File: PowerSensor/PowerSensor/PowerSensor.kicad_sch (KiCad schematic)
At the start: 14 parts, among them J1 Current Sens, J3 BAT+, J4 BAT-, J5 Screw_Terminal_01x04, U1 ACS712ELCTR-20A-T_NRND

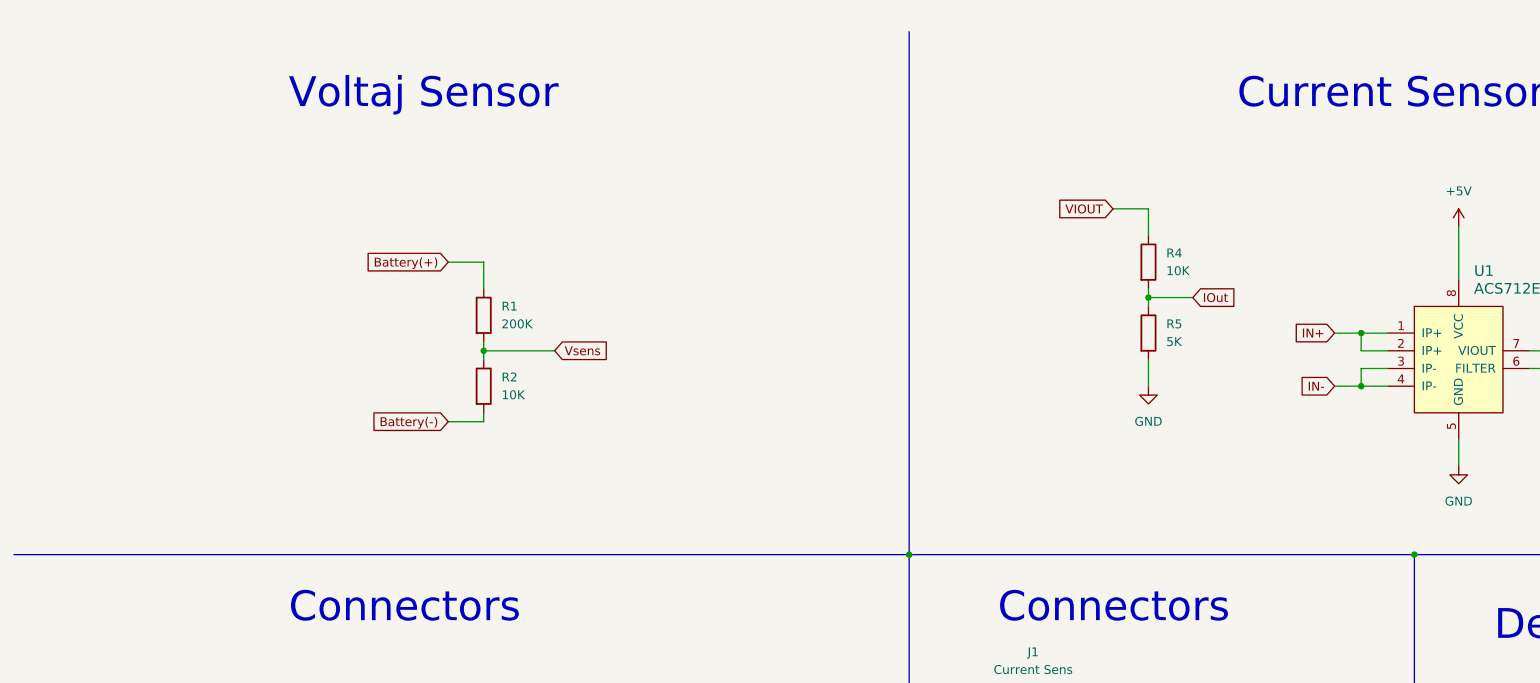
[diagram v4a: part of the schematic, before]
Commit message: Add discription for voltage divider
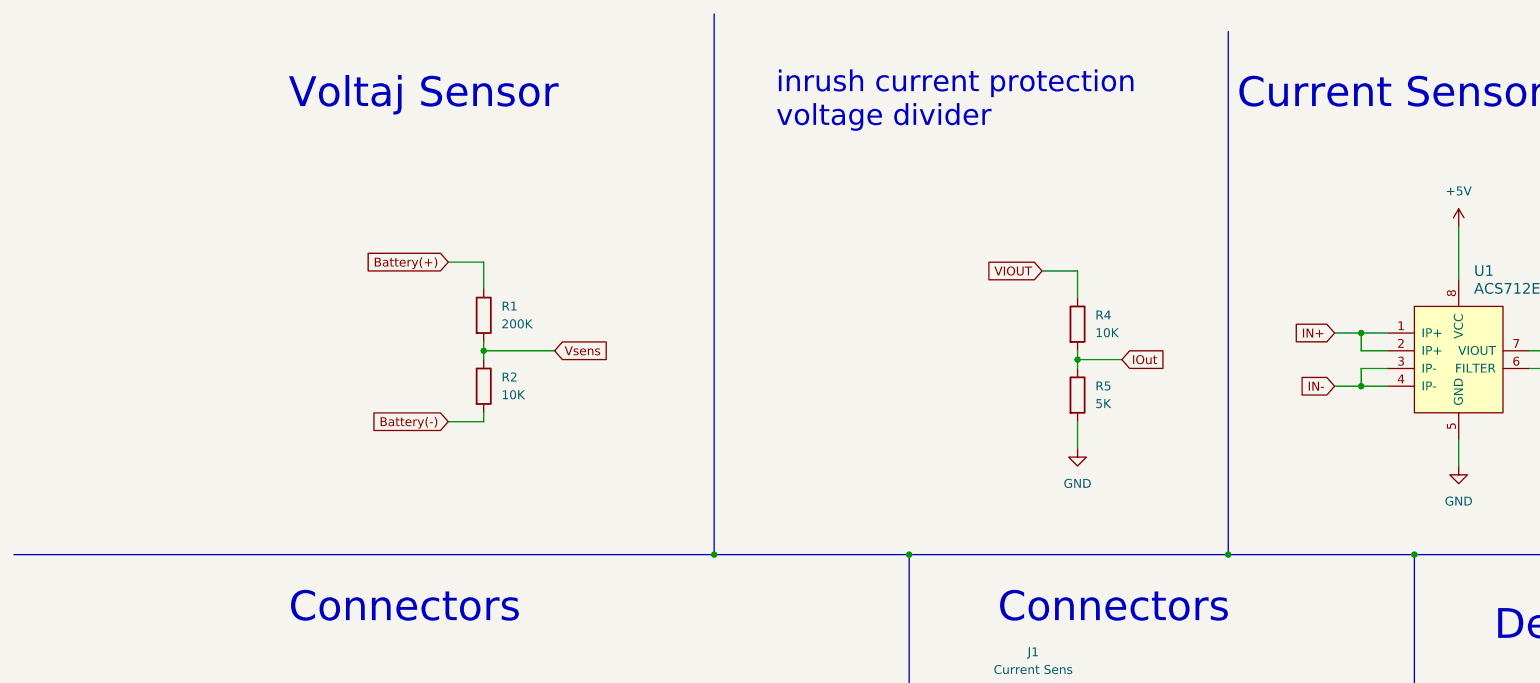
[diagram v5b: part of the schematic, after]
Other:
- note added: "inrush current protection voltage divider"
- moved on the sheet: R4, R5
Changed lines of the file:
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@@
   (junction (at 53.34 125.73) (diameter 0) (color 0 0 0 0)
   )
-  (junction (at 175.26 49.53) (diameter 0) (color 0 0 0 0)
+  (junction (at 165.1 58.42) (diameter 0) (color 0 0 0 0)
   )
   (junction (at 228.6 110.49) (diameter 0) (color 0 0 0 0)
@@
   (junction (at 205.74 54.61) (diameter 0) (color 0 0 0 0)
   )
+  (junction (at 186.69 86.36) (diameter 0) (color 0 0 0 0)
+  )
+  (junction (at 113.03 86.36) (diameter 0) (color 0 0 0 0)
+  )
   (junction (at 213.36 86.36) (diameter 0) (color 0 0 0 0)
   )
@@
     (stroke (width 0) (type default))
   )
-  (wire (pts (xy 175.26 49.53) (xy 181.61 49.53))
+  (wire (pts (xy 165.1 58.42) (xy 171.45 58.42))
     (stroke (width 0) (type default))
   )
@@
     (stroke (width 0) (type default))
   )
-  (wire (pts (xy 175.26 36.83) (xy 170.18 36.83))
+  (wire (pts (xy 165.1 45.72) (xy 160.02 45.72))
     (stroke (width 0) (type default))
   )
@@
     (stroke (width 0) (type default))
   )
+  (bus (pts (xy 113.03 86.36) (xy 140.97 86.36))
+    (stroke (width 0) (type dash_dot))
+  )
   (bus (pts (xy 140.97 86.36) (xy 140.97 198.12))
     (stroke (width 0) (type dash_dot))
@@
     (stroke (width 0) (type default))
   )
-  (bus (pts (xy 140.97 86.36) (xy 213.36 86.36))
-    (stroke (width 0) (type dash_dot))
-  )
-  (bus (pts (xy 140.97 11.43) (xy 140.97 86.36))
+  (bus (pts (xy 140.97 86.36) (xy 186.69 86.36))
+    (stroke (width 0) (type dash_dot))
+  )
+  (bus (pts (xy 113.03 8.89) (xy 113.03 86.36))
     (stroke (width 0) (type dash_dot))
   )
@@
     (stroke (width 0) (type default))
   )
+  (bus (pts (xy 186.69 11.43) (xy 186.69 86.36))
+    (stroke (width 0) (type dash_dot))
+  )
   (wire (pts (xy 205.74 59.69) (xy 205.74 62.23))
     (stroke (width 0) (type default))
@@
     (stroke (width 0) (type default))
   )
-  (wire (pts (xy 175.26 40.64) (xy 175.26 36.83))
-    (stroke (width 0) (type default))
-  )
-  (wire (pts (xy 175.26 58.42) (xy 175.26 62.23))
+  (wire (pts (xy 165.1 49.53) (xy 165.1 45.72))
+    (stroke (width 0) (type default))
+  )
+  (wire (pts (xy 165.1 67.31) (xy 165.1 71.12))
     (stroke (width 0) (type default))
   )
@@
     (stroke (width 0) (type default))
   )
-  (bus (pts (xy 12.7 86.36) (xy 140.97 86.36))
+  (bus (pts (xy 12.7 86.36) (xy 113.03 86.36))
     (stroke (width 0) (type dash_dot))
   )
@@
     (stroke (width 0) (type default))
   )
-  (wire (pts (xy 175.26 49.53) (xy 175.26 50.8))
+  (bus (pts (xy 186.69 86.36) (xy 213.36 86.36))
+    (stroke (width 0) (type dash_dot))
+  )
+  (wire (pts (xy 165.1 58.42) (xy 165.1 59.69))
     (stroke (width 0) (type default))
   )
@@
     (stroke (width 0) (type default))
   )
-  (wire (pts (xy 175.26 48.26) (xy 175.26 49.53))
+  (wire (pts (xy 165.1 57.15) (xy 165.1 58.42))
     (stroke (width 0) (type default))
   )
@@
   (text "Power LED\n" (at 233.68 139.7 0)
     (effects (font (size 4.27 4.27) (color 32 32 255 1)) (justify left bottom))
+  )
+  (text "inrush current protection \nvoltage divider" (at 121.92 25.4 0)
+    (effects (font (size 3 3) (color 26 18 255 1)) (justify left bottom))
   )
   (text "Voltaj Sensor" (at 52.07 22.86 0)
@@
     )
   )
-  (global_label "IOut" (shape input) (at 181.61 49.53 0) (fields_autoplaced)
-    (effects (font (size 1.27 1.27)) (justify left))
-    (property "Intersheetrefs" "${INTERSHEET_REFS}" (at 188.4052 49.53 0)
+  (global_label "IOut" (shape input) (at 171.45 58.42 0) (fields_autoplaced)
+    (effects (font (size 1.27 1.27)) (justify left))
+    (property "Intersheetrefs" "${INTERSHEET_REFS}" (at 178.2452 58.42 0)
       (effects (font (size 1.27 1.27)) (justify left) hide)
     )
@@
     )
   )
-  (global_label "VIOUT" (shape input) (at 170.18 36.83 180) (fields_autoplaced)
+  (global_label "VIOUT" (shape input) (at 160.02 45.72 180) (fields_autoplaced)
     (effects (font (size 1.27 1.27)) (justify right))
-    (property "Intersheetrefs" "${INTERSHEET_REFS}" (at 161.8728 36.83 0)
+    (property "Intersheetrefs" "${INTERSHEET_REFS}" (at 151.7128 45.72 0)
       (effects (font (size 1.27 1.27)) (justify right) hide)
     )
@@
     )
   )
-  (symbol (lib_id "Device:R") (at 175.26 54.61 0) (unit 1)
-    (in_bom yes) (on_board yes) (dnp no) (fields_autoplaced)
-    (property "Reference" "R5" (at 177.8 53.34 0)
-      (effects (font (size 1.27 1.27)) (justify left))
-    )
-    (property "Value" "5K" (at 177.8 55.88 0)
-      (effects (font (size 1.27 1.27)) (justify left))
-    )
-    (property "Footprint" "Resistor_SMD:R_0805_2012Metric" (at 173.482 54.61 90)
-      (effects (font (size 1.27 1.27)) hide)
-    )
-    (property "Datasheet" "~" (at 175.26 54.61 0)
+  (symbol (lib_id "Device:R") (at 165.1 63.5 0) (unit 1)
+    (in_bom yes) (on_board yes) (dnp no) (fields_autoplaced)
+    (property "Reference" "R5" (at 167.64 62.23 0)
+      (effects (font (size 1.27 1.27)) (justify left))
+    )
+    (property "Value" "5K" (at 167.64 64.77 0)
+      (effects (font (size 1.27 1.27)) (justify left))
+    )
+    (property "Footprint" "Resistor_SMD:R_0805_2012Metric" (at 163.322 63.5 90)
+      (effects (font (size 1.27 1.27)) hide)
+    )
+    (property "Datasheet" "~" (at 165.1 63.5 0)
       (effects (font (size 1.27 1.27)) hide)
     )
@@
     )
   )
-  (symbol (lib_id "Device:R") (at 175.26 44.45 0) (unit 1)
-    (in_bom yes) (on_board yes) (dnp no) (fields_autoplaced)
-    (property "Reference" "R4" (at 177.8 43.18 0)
-      (effects (font (size 1.27 1.27)) (justify left))
-    )
-    (property "Value" "10K" (at 177.8 45.72 0)
-      (effects (font (size 1.27 1.27)) (justify left))
-    )
-    (property "Footprint" "Resistor_SMD:R_0805_2012Metric" (at 173.482 44.45 90)
-      (effects (font (size 1.27 1.27)) hide)
-    )
-    (property "Datasheet" "~" (at 175.26 44.45 0)
+  (symbol (lib_id "Device:R") (at 165.1 53.34 0) (unit 1)
+    (in_bom yes) (on_board yes) (dnp no) (fields_autoplaced)
+    (property "Reference" "R4" (at 167.64 52.07 0)
+      (effects (font (size 1.27 1.27)) (justify left))
+    )
+    (property "Value" "10K" (at 167.64 54.61 0)
+      (effects (font (size 1.27 1.27)) (justify left))
+    )
+    (property "Footprint" "Resistor_SMD:R_0805_2012Metric" (at 163.322 53.34 90)
+      (effects (font (size 1.27 1.27)) hide)
+    )
+    (property "Datasheet" "~" (at 165.1 53.34 0)
       (effects (font (size 1.27 1.27)) hide)
     )
@@
     )
   )
-  (symbol (lib_id "power:GND") (at 175.26 62.23 0) (unit 1)
-    (in_bom yes) (on_board yes) (dnp no) (fields_autoplaced)
-    (property "Reference" "#PWR08" (at 175.26 68.58 0)
-      (effects (font (size 1.27 1.27)) hide)
-    )
-    (property "Value" "GND" (at 175.26 67.31 0)
-      (effects (font (size 1.27 1.27)))
-    )
-    (property "Footprint" "" (at 175.26 62.23 0)
-      (effects (font (size 1.27 1.27)) hide)
-    )
-    (property "Datasheet" "" (at 175.26 62.23 0)
-      (effects (font (size 1.27 1.27)) hide)
-    )
+  (symbol (lib_id "power:GND") (at 165.1 71.12 0) (unit 1)
+    (in_bom yes) (on_board yes) (dnp no) (fields_autoplaced)
+    (property "Reference" "#PWR08" (at 165.1 77.47 0)
+      (effects (font (size 1.27 1.27)) hide)
+    )
+    (property "Value" "GND" (at 165.1 76.2 0)
+      (effects (font (size 1.27 1.27)))
+    )
+    (property "Footprint" "" (at 165.1 71.12 0)
+      (effects (font (size 1.27 1.27)) hide)
+    )
+    (property "Datasheet" "" (at 165.1 71.12 0)
+      (effects (font (size 1.27 1.27)) hide)
+    )
